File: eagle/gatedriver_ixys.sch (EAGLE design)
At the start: 45 parts, among them K1 G5V-2, X4 BU-SMA-V

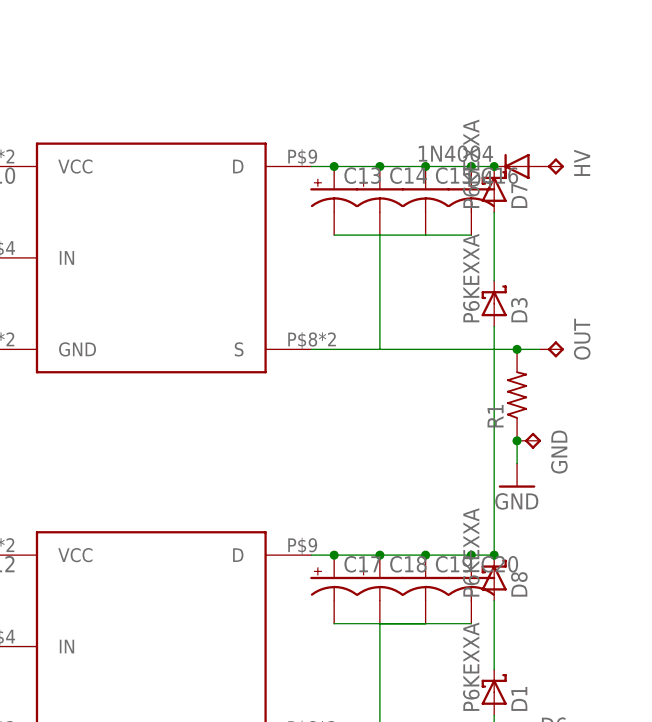
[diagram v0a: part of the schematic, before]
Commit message: capacitor bank
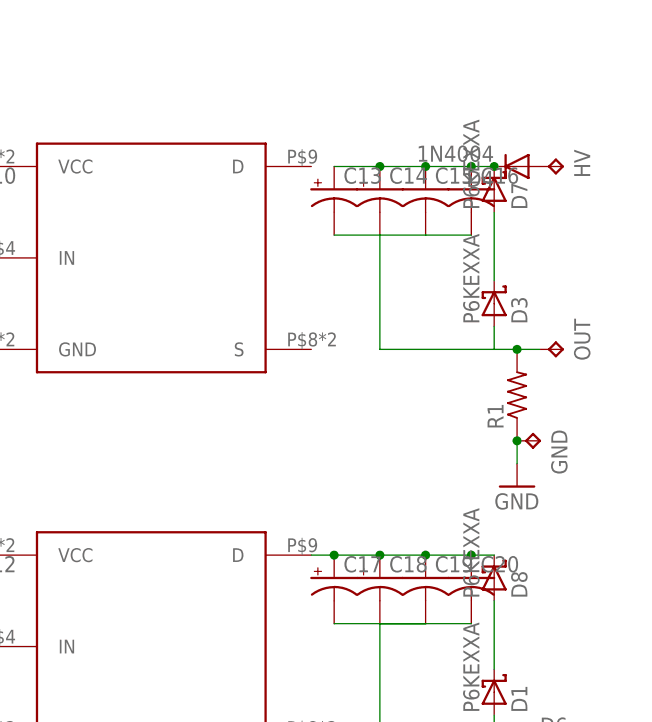
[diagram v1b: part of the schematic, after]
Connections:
- new net N$22: C17.+, C18.+, C19.1, C20.1, D8.C, U$9.D
- net N$17: no longer U$8.D
- net N$21: no longer C17.+, C18.+, C19.1, C20.1, D8.C, U$8.S, U$9.D
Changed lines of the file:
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@@
 <net name="N$17" class="0">
 <segment>
-<pinref part="U$8" gate="G$1" pin="D"/>
 <pinref part="D4" gate="1" pin="C"/>
 <wire x1="162.56" y1="12.7" x2="167.64" y2="12.7" width="0.1524" layer="91"/>
@@
 <pinref part="C14" gate="G$1" pin="+"/>
 <wire x1="162.56" y1="12.7" x2="157.48" y2="12.7" width="0.1524" layer="91"/>
-<junction x="157.48" y="12.7"/>
 <pinref part="C15" gate="G$1" pin="1"/>
 <junction x="167.64" y="12.7"/>
 <pinref part="C16" gate="G$1" pin="1"/>
 <junction x="172.72" y="12.7"/>
-<wire x1="157.48" y1="12.7" x2="154.94" y2="12.7" width="0.1524" layer="91"/>
 <pinref part="D7" gate="1" pin="C"/>
 <junction x="175.26" y="12.7"/>
@@
 <pinref part="D3" gate="1" pin="A"/>
 <wire x1="175.26" y1="-5.08" x2="175.26" y2="-7.62" width="0.1524" layer="91"/>
-<pinref part="U$8" gate="G$1" pin="S"/>
 <wire x1="175.26" y1="-7.62" x2="162.56" y2="-7.62" width="0.1524" layer="91"/>
 <pinref part="OUT" gate="G$1" pin="TP"/>
-<wire x1="162.56" y1="-7.62" x2="154.94" y2="-7.62" width="0.1524" layer="91"/>
 <wire x1="175.26" y1="-7.62" x2="177.8" y2="-7.62" width="0.1524" layer="91"/>
-<pinref part="U$9" gate="G$1" pin="D"/>
 <wire x1="177.8" y1="-7.62" x2="180.34" y2="-7.62" width="0.1524" layer="91"/>
-<wire x1="154.94" y1="-30.48" x2="157.48" y2="-30.48" width="0.1524" layer="91"/>
-<wire x1="157.48" y1="-30.48" x2="162.56" y2="-30.48" width="0.1524" layer="91"/>
-<wire x1="162.56" y1="-30.48" x2="167.64" y2="-30.48" width="0.1524" layer="91"/>
-<wire x1="167.64" y1="-30.48" x2="172.72" y2="-30.48" width="0.1524" layer="91"/>
-<wire x1="172.72" y1="-30.48" x2="175.26" y2="-30.48" width="0.1524" layer="91"/>
-<wire x1="175.26" y1="-30.48" x2="175.26" y2="-7.62" width="0.1524" layer="91"/>
 <pinref part="R1" gate="G$1" pin="2"/>
 <junction x="177.8" y="-7.62"/>
 <wire x1="167.64" y1="5.08" x2="162.56" y2="5.08" width="0.1524" layer="91"/>
 <wire x1="162.56" y1="5.08" x2="162.56" y2="-7.62" width="0.1524" layer="91"/>
-<pinref part="C17" gate="G$1" pin="+"/>
-<junction x="157.48" y="-30.48"/>
-<pinref part="C18" gate="G$1" pin="+"/>
-<junction x="162.56" y="-30.48"/>
-<pinref part="C19" gate="G$1" pin="1"/>
-<junction x="167.64" y="-30.48"/>
-<pinref part="C20" gate="G$1" pin="1"/>
-<junction x="172.72" y="-30.48"/>
-<pinref part="D8" gate="1" pin="C"/>
-<junction x="175.26" y="-30.48"/>
 </segment>
 </net>
@@
 </segment>
 </net>
+<net name="N$22" class="0">
+<segment>
+<pinref part="D8" gate="1" pin="C"/>
+<wire x1="172.72" y1="-30.48" x2="175.26" y2="-30.48" width="0.1524" layer="91"/>
+<pinref part="C20" gate="G$1" pin="1"/>
+<junction x="172.72" y="-30.48"/>
+<wire x1="167.64" y1="-30.48" x2="172.72" y2="-30.48" width="0.1524" layer="91"/>
+<pinref part="C19" gate="G$1" pin="1"/>
+<junction x="167.64" y="-30.48"/>
+<wire x1="162.56" y1="-30.48" x2="167.64" y2="-30.48" width="0.1524" layer="91"/>
+<pinref part="C18" gate="G$1" pin="+"/>
+<junction x="162.56" y="-30.48"/>
+<wire x1="157.48" y1="-30.48" x2="162.56" y2="-30.48" width="0.1524" layer="91"/>
+<pinref part="C17" gate="G$1" pin="+"/>
+<junction x="157.48" y="-30.48"/>
+<pinref part="U$9" gate="G$1" pin="D"/>
+<wire x1="154.94" y1="-30.48" x2="157.48" y2="-30.48" width="0.1524" layer="91"/>
+</segment>
+</net>

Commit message: IXYS board solution, gatedriver components
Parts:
- removed D4, D6: 1N4004, diode:1N4004
- added C21, C22: (no value), rcl:C-US102-064X133
- added R2: (no value), resistor:R-US_0207/15
- added R3: (no value), resistor:R-US_0207/12
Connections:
- removed net N$13: C11.-, C12.2, C7.-, C8.2, D5.A, DC2.0V, U$2.S3, U$9.GND
- removed net N$20: C10.2, C5.-, C6.2, C9.-, D2.A, DC1.0V, U$1.S3, U$8.GND
- removed net N$22: C17.+, C18.+, C19.1, C20.1, D8.C, U$9.D
- net GND: now also C21.2, C22.2
- net N$16: now also C3.2, R2.1; no longer D4.A, HV.TP
- net N$17: now also C21.1, HV.TP, U$8.D; no longer D4.C
- net N$19: now also C11.-, C12.2, C22.1, C7.-, C8.2, D5.A, DC2.0V, LV.TP, U$2.S3, U$9.GND; no longer D6.A
- net N$21: now also C10.2, C17.+, C18.+, C19.1, C20.1, C5.-, C6.2, C9.-, D2.A, D8.C, DC1.0V, U$1.S3, U$8.GND, U$8.S, U$9.D
- net N$3: now also R2.2; no longer C3.2
- net N$5: now also R3.2; no longer C4.2
- net N$6: now also C4.2, R3.1; no longer D6.C, LV.TP
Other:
- moved on the sheet: C1, C10, C11, C12, C13, C15, C16, C17, C19, C2, C20, C3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

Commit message: layout fixes
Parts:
- R1: device resistor:R-US_0207/10 -> resistor:R-US_0414/15
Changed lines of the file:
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@@
 <part name="C11" library="rcl" deviceset="CPOL-US" device="E5-10.5"/>
 <part name="C12" library="resistor" deviceset="C-US" device="050-075X075"/>
-<part name="R1" library="resistor" deviceset="R-US_" device="0207/10"/>
+<part name="R1" library="resistor" deviceset="R-US_" device="0414/15"/>
 <part name="C13" library="rcl" deviceset="CPOL-US" device="E5-10.5"/>
 <part name="C14" library="rcl" deviceset="CPOL-US" device="E5-10.5"/>

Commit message: timing ctia
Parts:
- added C23: (no value), rcl:C-US102-064X133
- added D4, D6: 1N4148DO35-10, diode:1N4148DO35-10
- added GND15, GND16: TPPAD1-20Y, testpad:TPPAD1-20Y
- added R4, R5: (no value), resistor:R-US_0207/10
- added R6, R7: (no value), resistor:R-US_0414/15
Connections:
- removed net N$25: C2.2, D5.C, U$9.IN
- new net GD_HI: D4.A, R4.2, U$8.IN
- new net GD_LO: D6.A, R5.2, U$9.IN
- new net N$13: C23.1, R7.1
- new net N$20: C1.2, D2.C, D4.C, R4.1
- new net OUT: C10.2, C13.-, C14.-, C15.2, C16.2, C17.+, C18.+, C19.1, C20.1, C5.-, C6.2, C9.-, D2.A, D3.A, D8.C, DC1.0V, OUT.TP, R1.2, R7.2, U$1.S3, U$8.GND, U$8.S, U$9.D
- net GND: now also C23.2, GND15.TP, GND16.TP, R6.1; no longer R1.1
- net N$12: now also R1.1, R6.2; no longer C1.2, D2.C, U$8.IN
- net N$21: now also C2.2, D5.C, D6.C, R5.1; no longer C10.2, C13.-, C14.-, C15.2, C16.2, C17.+, C18.+, C19.1, C20.1, C5.-, C6.2, C9.-, D2.A, D3.A, D8.C, DC1.0V, OUT.TP, R1.2, U$1.S3, U$8.GND, U$8.S, U$9.D
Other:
- moved on the sheet: C10, C11, C12, C6, C8, C9, D1, D3, D8, GND
